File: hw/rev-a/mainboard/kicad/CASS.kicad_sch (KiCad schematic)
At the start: 19 parts, among them J13 CASS_B_HEADER, J20 CASS_A_HEADER, J3 CASS A, J6 CASS B, Q2 AO3401A, Q3 AO3401A

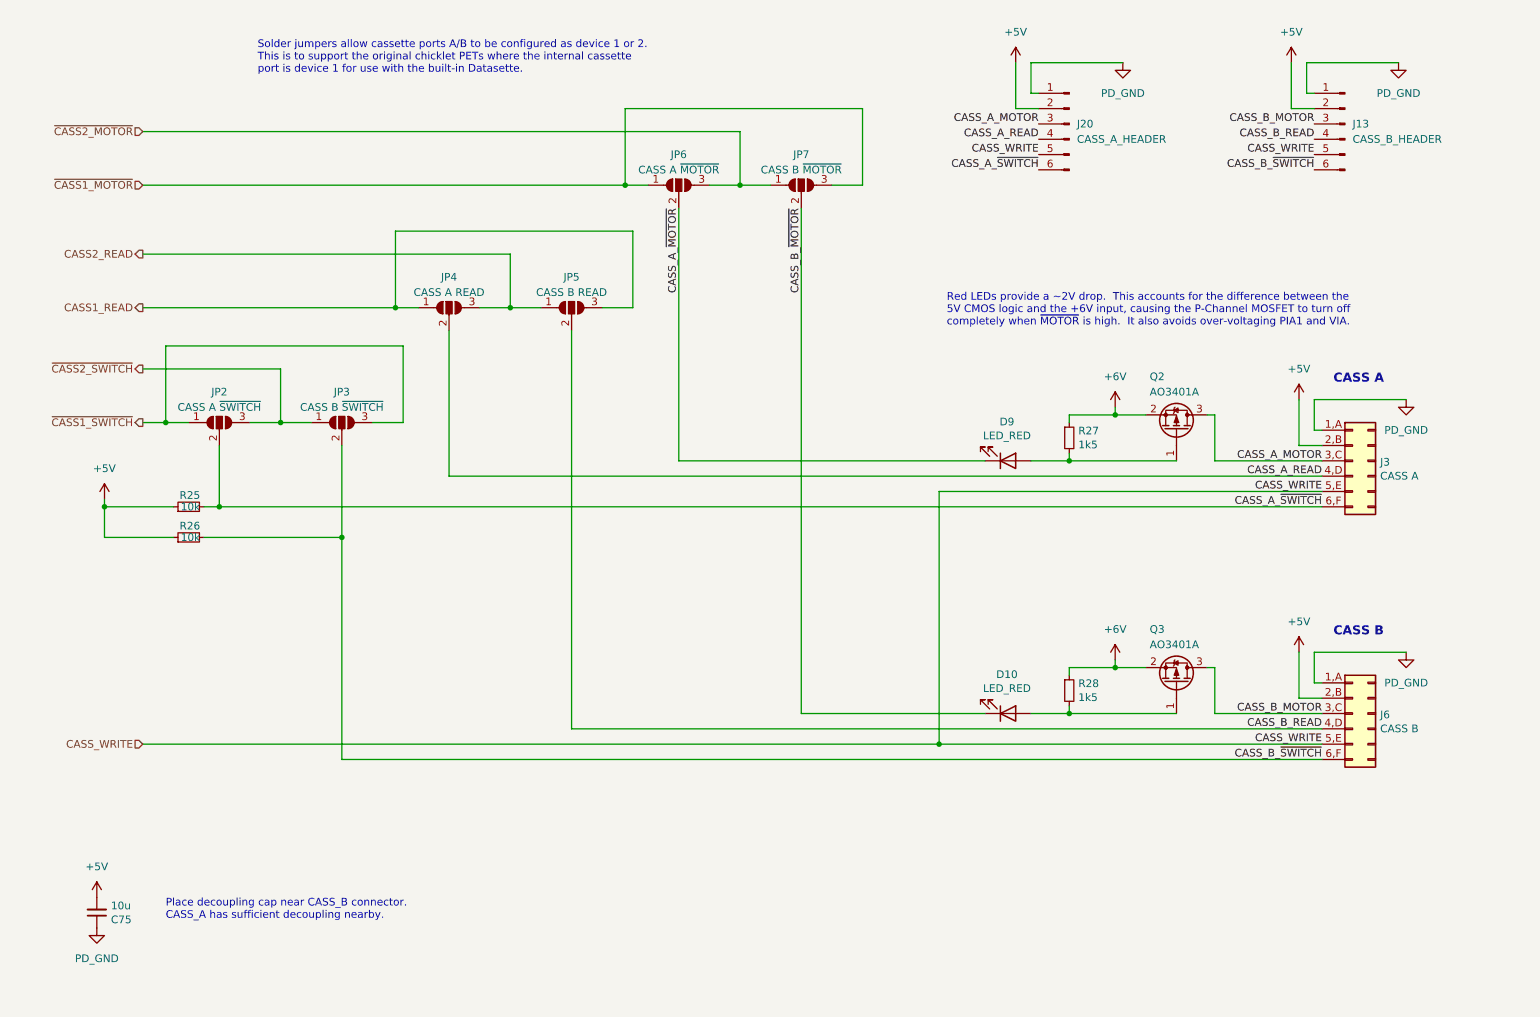
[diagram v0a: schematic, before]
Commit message: hw: ren rev-c -> rev-a
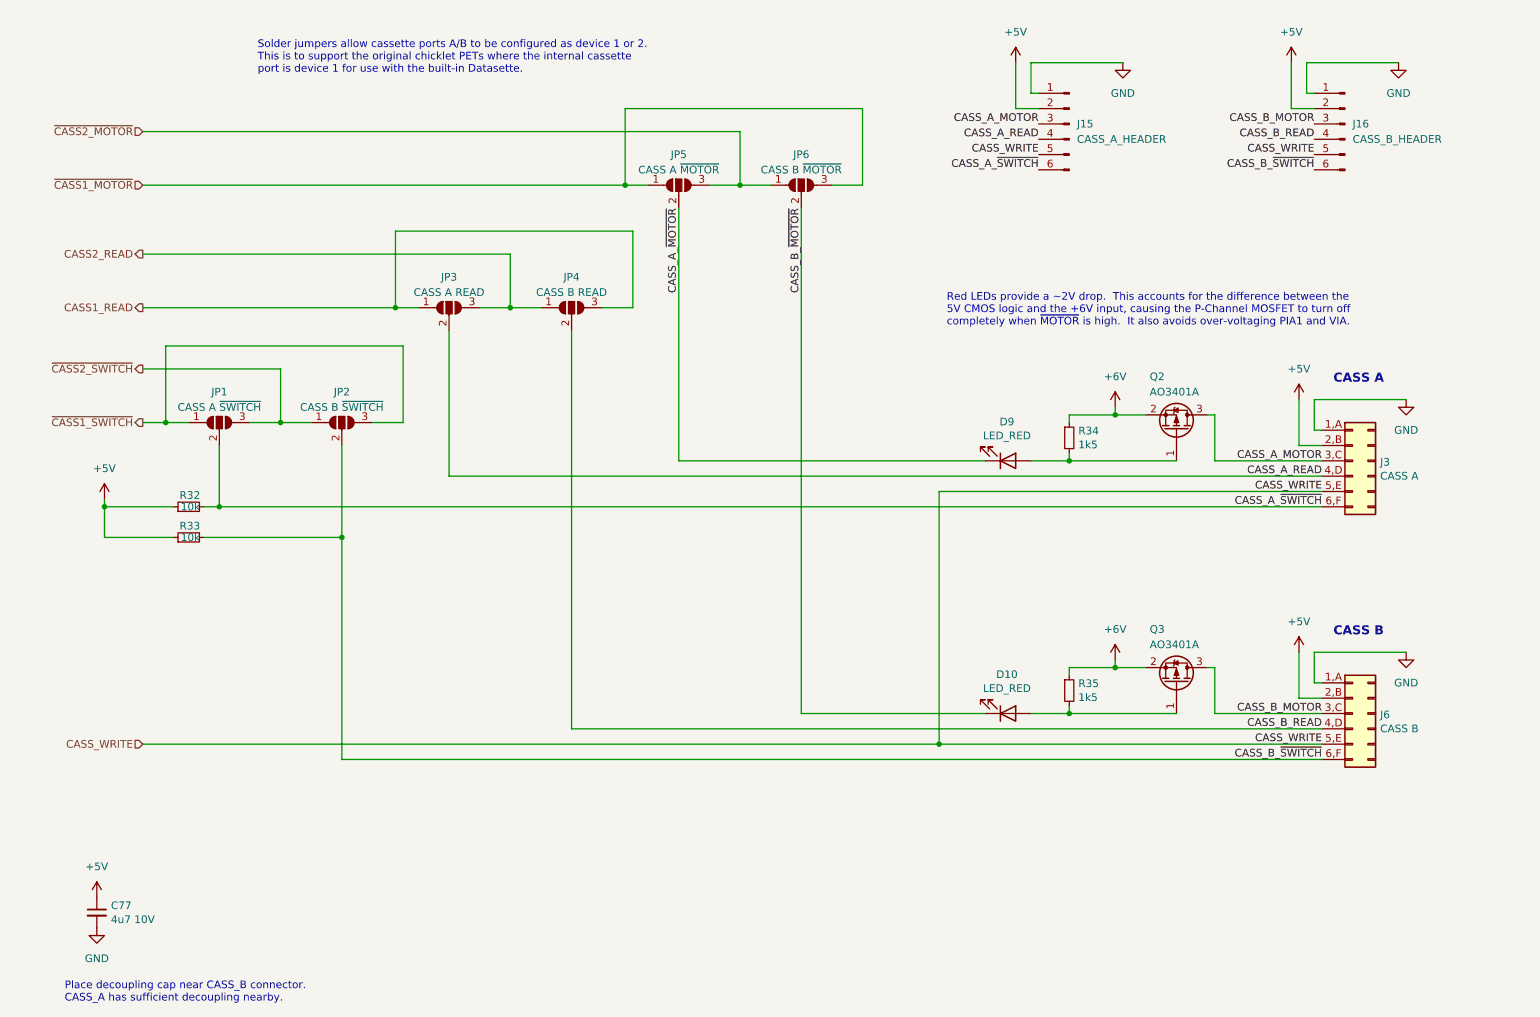
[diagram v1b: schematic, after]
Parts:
- removed C75: 10u, Capacitor_SMD:C_0603_1608Metric, symbol Device:C_Small
- added C77: 4u7 10V, Capacitor_SMD:C_0402_1005Metric, symbol Device:C_Small
- J15: renamed from J20; symbol Connector:Conn_01x06_Male -> Connector:Conn_01x06_Pin
- J16: renamed from J13; symbol Connector:Conn_01x06_Male -> Connector:Conn_01x06_Pin
- J3, J6: footprint Retrocomputing:CBM_PET_CASS_EDGE_CON_12P -> EconoPET:CBM_PET_CASS_EDGE_CON_12P; symbol Retrocomputing:CBM_PET_CASS_Conn_01x06_Card_Edge -> EconoPET:CBM_PET_CASS_Conn_01x06_Card_Edge
- Q2, Q3: footprint JLCPCB:SOT-23_L2.9-W1.3-P1.90-LS2.4-BR -> EconoPET:SOT-23_L2.9-W1.3-P1.90-LS2.4-BR
- renumbered JP2 to JP1, JP3 to JP2, JP4 to JP3, JP5 to JP4, JP6 to JP5, JP7 to JP6, R25 to R32, R26 to R33, R27 to R34, R28 to R35
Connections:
- net +5V: now also C77.1
- net PD_GND renamed GND
- net GND: now also C77.2

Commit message: hw: tidy schematics for publication
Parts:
- J3: value CASS A -> CASS_A_EDGE
- J6: value CASS B -> CASS_B_EDGE
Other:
- note added: "CASSETTE PORTS"
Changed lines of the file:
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@@
 		(date "2023-10-01")
 		(rev "A")
+		(comment 1 "Unspecified resistors are 1% and rated for 62.5mW or higher")
+		(comment 2 "Unspecified capacitors are rated for 25V or higher")
+		(comment 3 "Signals with B-prefix are level-shifted from 3V3 to 5V")
 	)
 	(junction
@@
 	(text "Solder jumpers allow cassette ports A/B to be configured as device 1 or 2.\nThis is to support the original chicklet PETs where the internal cassette\nport is device 1 for use with the built-in Datasette.\n"
 		(exclude_from_sim no)
-		(at 60.96 36.195 0)
+		(at 64.77 36.83 0)
 		(effects
 			(font
@@
 			(font
 				(size 1.27 1.27)
+			)
+			(justify left bottom)
+		)
+	)
+	(text "CASSETTE PORTS"
+		(exclude_from_sim no)
+		(at 64.77 28.575 0)
+		(effects
+			(font
+				(size 1.5 1.5)
+				(thickness 0.8)
+				(bold yes)
 			)
 			(justify left bottom)
@@
 			)
 		)
-		(property "Value" "CASS B"
+		(property "Value" "CASS_B_EDGE"
 			(at 247.142 144.7546 0)
 			(effects
@@
 			)
 		)
-		(property "Value" "CASS A"
+		(property "Value" "CASS_A_EDGE"
 			(at 247.142 102.8446 0)
 			(effects

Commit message: hw: tidy schematics for publication
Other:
- company: (none) -> https://is.gd/6hpvh6
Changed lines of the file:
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@@
 		(date "2023-10-01")
 		(rev "A")
-		(comment 1 "Unspecified resistors are 1% and rated for 62.5mW or higher")
-		(comment 2 "Unspecified capacitors are rated for 25V or higher")
+		(company "https://is.gd/6hpvh6")
+		(comment 1 "Unspecified resistors are 1% / 62.5mW")
+		(comment 2 "Unspecified capacitors are 25V")
 		(comment 3 "Signals with B-prefix are level-shifted from 3V3 to 5V")
+		(comment 4 "License: CC0 1.0 Universal (Public Domain Dedication)")
 	)
 	(junction
